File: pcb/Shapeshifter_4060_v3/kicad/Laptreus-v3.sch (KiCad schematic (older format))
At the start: 96 parts, among them SW1 TAB, SW10 O, SW11 P, SW12 BKSP, SW13 ESC, SW14 A, SW15 S, SW16 D, SW17 F, SW18 G, SW19 H, SW2 Q, SW20 J, SW21 K, SW22 L, SW23 ;, SW24 ENTER, SW25 SHIFT, SW26 Z, SW27 X, SW28 C, SW29 V, SW3 W, SW30 B, SW31 N, SW32 M, SW33 ,, SW34 ., SW35 /, SW36 SHIFT, SW37 CTRL/ESC, SW38 ALT/GRV, SW39 CMD, SW4 E, SW40 FN1, SW41 SHIFT, SW42 BKSP, SW43 ENTER, SW44 SPACE, SW45 LEFT, SW46 DOWN, SW47 UP, SW48 RIGHT, SW5 R, SW6 T, SW7 Y, SW8 U, SW9 I

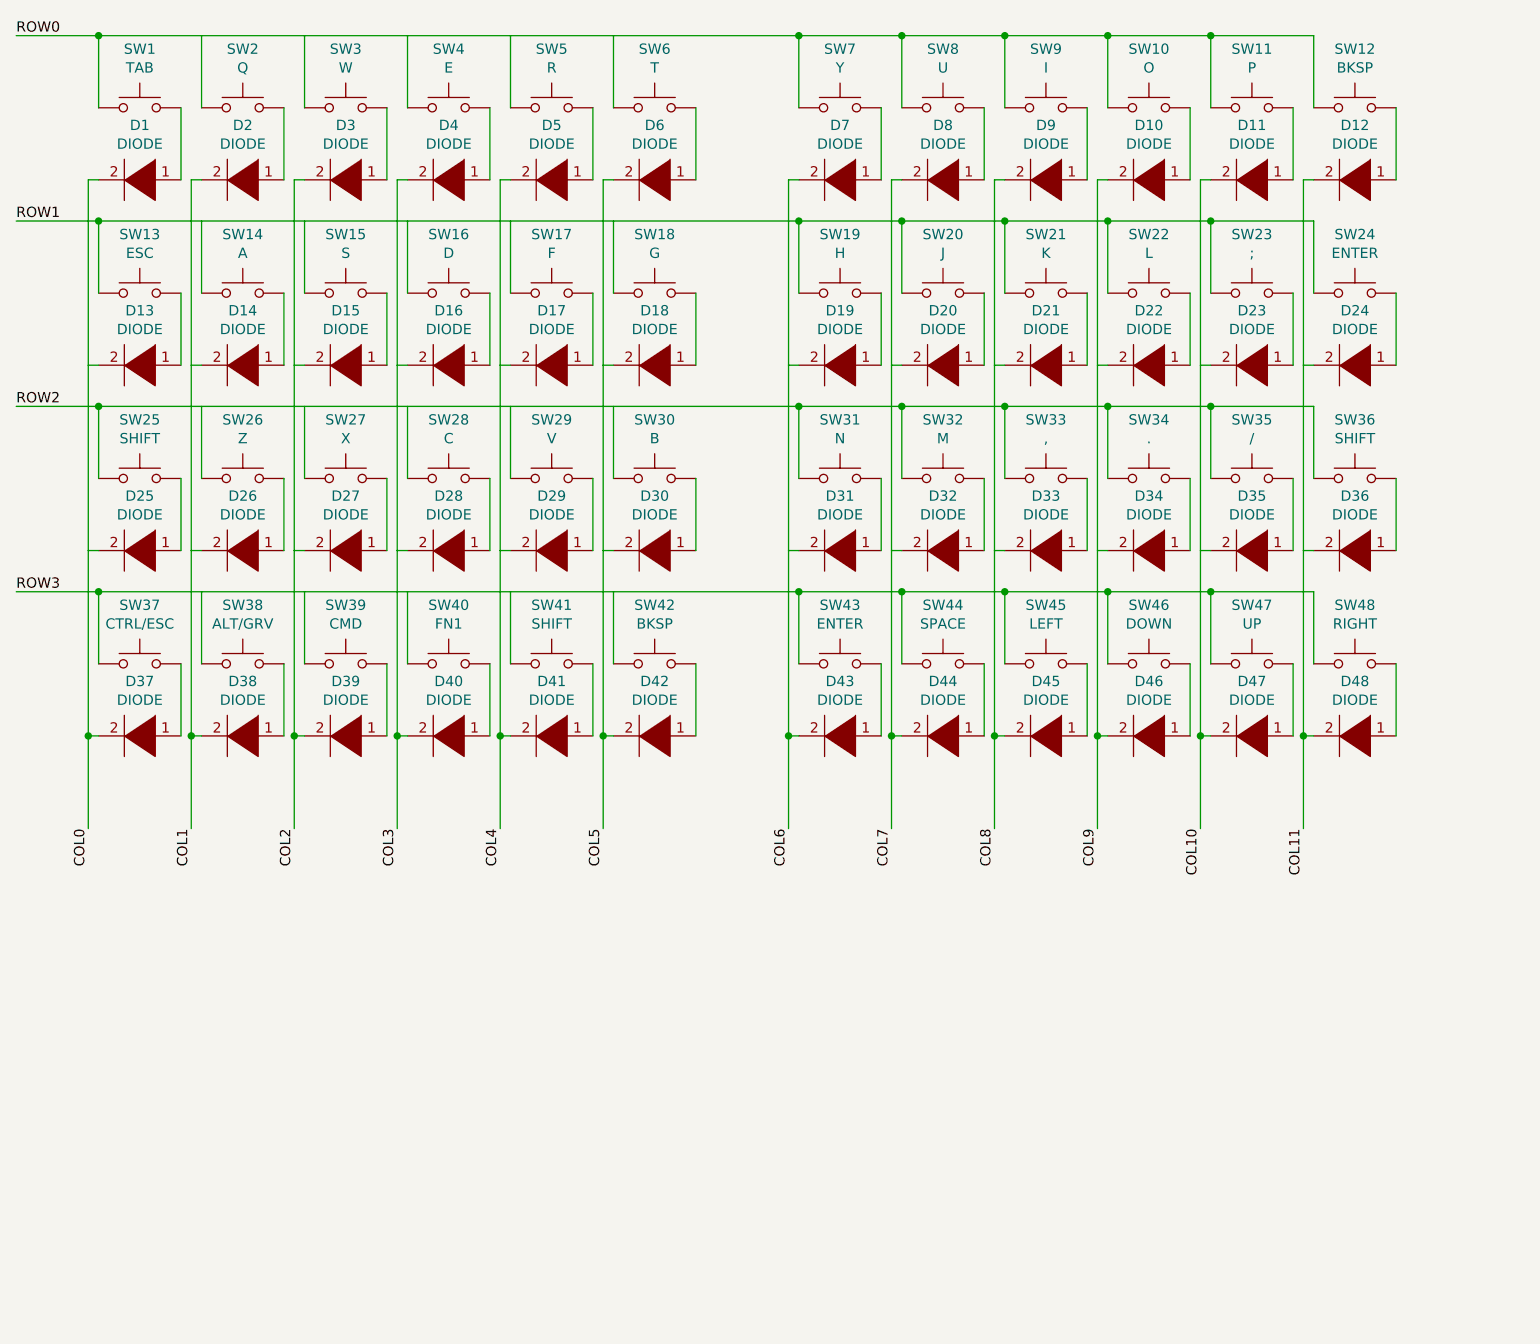
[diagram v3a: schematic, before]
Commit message: added fids/jumpers to schematic, fixed wiring typo, added pro micro fo otprint
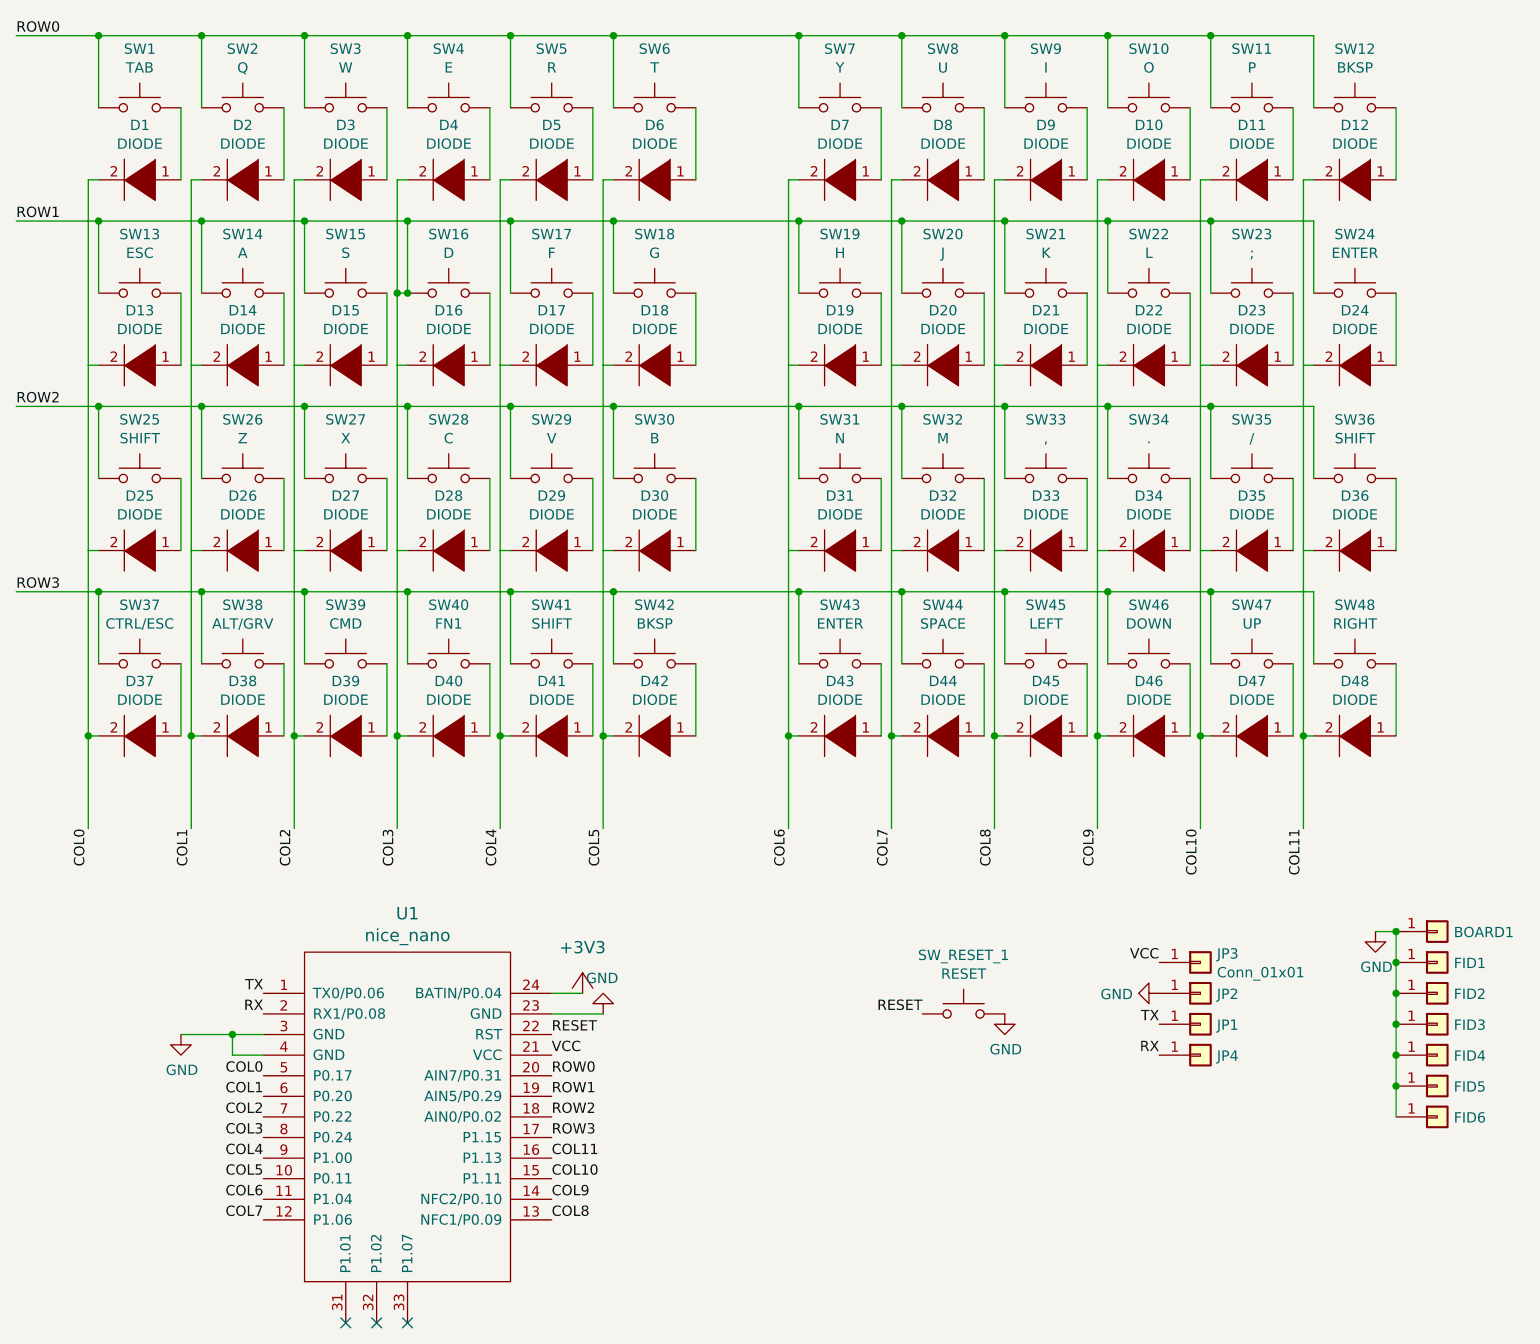
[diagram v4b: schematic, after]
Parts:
- added BOARD1: Conn_01x01, Kitsune-Footprints:60_percent_plus_tofu_no_center_holes, symbol Connector_Generic:Conn_01x01
- added FID1, FID2, FID3, FID4, FID5, FID6: Conn_01x01, Kitsune-Footprints:FIDUCIAL, symbol Connector_Generic:Conn_01x01
- added JP1, JP2, JP3, JP4: Conn_01x01, Kitsune-Footprints:1X01-CLEANBIG, symbol Connector_Generic:Conn_01x01
- added SW_RESET_1: RESET, Kitsune-Footprints:SW_SPST_B3U-1000P, symbol Kitsune-Symbols:SW_Push
- added U1: nice_nano, Kitsune-Footprints:nice_nano, symbol nice_nano:nice_nano
- SW13, SW14, SW23, SW24: footprint Kitsune-Footprints:Hybrid_Kailh_MX_Choc_Socket_Through_Hole_With_Diode -> Kitsune-Footprints:Hybrid_Kailh_MX_Choc_Socket_Through_Hole_With_Diode_No_Diode_Trace
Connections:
- net labels added: +3V3, GND, RESET, RX, TX, VCC
- wire segments 220 -> 255
- no-connect marks 0 -> 3

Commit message: Add nomask variant of nice nano, remove adhesives, add reset switch
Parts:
- SW13: footprint Kitsune-Footprints:Hybrid_Kailh_MX_Choc_Socket_Through_Hole_With_Diode_No_Diode_Trace -> Kitsune-Footprints:Hybrid_Kailh_MX_Choc_Socket_Through_Hole_With_Diode
- U1: footprint Kitsune-Footprints:nice_nano -> Kitsune-Footprints:nice_nano_no_Bcu_mask
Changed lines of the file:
@@
 F 0 "SW13" H 1500 2435 50  0000 C CNN
 F 1 "ESC" H 1500 2344 50  0000 C CNN
-F 2 "Kitsune-Footprints:Hybrid_Kailh_MX_Choc_Socket_Through_Hole_With_Diode_No_Diode_Trace" H 1500 2350 50  0001 C CNN
+F 2 "Kitsune-Footprints:Hybrid_Kailh_MX_Choc_Socket_Through_Hole_With_Diode" H 1500 2350 50  0001 C CNN
 F 3 "~" H 1500 2350 50  0001 C CNN
 	1    1500 2150
@@
 F 0 "U1" H 2800 7037 60  0000 C CNN
 F 1 "nice_nano" H 2800 6931 60  0000 C CNN
-F 2 "Kitsune-Footprints:nice_nano" V 3850 3600 60  0001 C CNN
+F 2 "Kitsune-Footprints:nice_nano_no_Bcu_mask" V 3850 3600 60  0001 C CNN
 F 3 "" V 3850 3600 60  0001 C CNN
 	1    2800 6100

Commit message: all components wired up!
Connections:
- net COL0: now also U1.6 (P0.20); no longer U1.5 (P0.17)
- net COL1: now also U1.5 (P0.17); no longer U1.6 (P0.20)
- net COL10: now also U1.8 (P0.24); no longer U1.15 (P1.11)
- net COL11: now also U1.7 (P0.22); no longer U1.16 (P1.13)
- net COL2: now also U1.16 (P1.13); no longer U1.7 (P0.22)
- net COL3: now also U1.15 (P1.11); no longer SW13.1, SW14.1, SW15.1, SW16.1, SW17.1, SW18.1, SW19.1, SW20.1, SW21.1, SW22.1, SW23.1, SW24.1, U1.19 (AIN5/P0.29), U1.8 (P0.24)
- net COL4: now also U1.14 (NFC2/P0.10); no longer U1.9 (P1.00)
- net COL5: now also U1.13 (NFC1/P0.09); no longer U1.10 (P0.11)
- net COL6: now also U1.12 (P1.06); no longer U1.11 (P1.04)
- net COL7: now also U1.11 (P1.04); no longer U1.12 (P1.06)
- net COL8: now also U1.10 (P0.11); no longer U1.13 (NFC1/P0.09)
- net COL9: now also U1.9 (P1.00); no longer U1.14 (NFC2/P0.10)
- new net ROW1: SW13.1, SW14.1, SW15.1, SW16.1, SW17.1, SW18.1, SW19.1, SW20.1, SW21.1, SW22.1, SW23.1, SW24.1, U1.19 (AIN5/P0.29)
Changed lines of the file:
@@
 Wire Wire Line
 	2800 1600 2750 1600
-Wire Wire Line
-	2750 1600 2750 2150
 $Comp
 L pspice:DIODE D5
@@
 	1    0    0    -1
 $EndComp
+Text Label 2100 6050 2    50   ~ 0
+COL0
 Text Label 2100 5950 2    50   ~ 0
-COL0
-Text Label 2100 6050 2    50   ~ 0
 COL1
+Text Label 3500 6350 0    50   ~ 0
+COL2
+Text Label 3500 6450 0    50   ~ 0
+COL3
+Text Label 3500 6550 0    50   ~ 0
+COL4
+Text Label 3500 6650 0    50   ~ 0
+COL5
+Text Label 2100 6650 2    50   ~ 0
+COL6
+Text Label 2100 6550 2    50   ~ 0
+COL7
+Text Label 2100 6450 2    50   ~ 0
+COL8
+Text Label 2100 6350 2    50   ~ 0
+COL9
+Text Label 2100 6250 2    50   ~ 0
+COL10
 Text Label 2100 6150 2    50   ~ 0
-COL2
-Text Label 2100 6250 2    50   ~ 0
-COL3
-Text Label 2100 6350 2    50   ~ 0
-COL4
-Text Label 2100 6450 2    50   ~ 0
-COL5
-Text Label 2100 6550 2    50   ~ 0
-COL6
-Text Label 2100 6650 2    50   ~ 0
-COL7
-Text Label 3500 6650 0    50   ~ 0
-COL8
-Text Label 3500 6550 0    50   ~ 0
-COL9
-Text Label 3500 6450 0    50   ~ 0
-COL10
-Text Label 3500 6350 0    50   ~ 0
 COL11
 Text Label 3500 6250 0    50   ~ 0
@@
 Connection ~ 2300 1800
 Wire Wire Line
-	2300 1800 2800 1800
-Wire Wire Line
-	2800 1800 2800 2150
-Wire Wire Line
-	2800 2150 2750 2150
-Connection ~ 2800 1800
-Wire Wire Line
-	2800 1800 3300 1800
-Connection ~ 2800 2150
-Connection ~ 2750 2150
-Wire Wire Line
-	2750 2150 2750 2500
-Wire Wire Line
 	3300 1800 3300 2150
 Connection ~ 3300 1800
@@
 	7500 5250 7600 5250
 Connection ~ 7600 5250
+Wire Wire Line
+	2300 1800 2800 1800
+Wire Wire Line
+	2750 1600 2750 2500
+Wire Wire Line
+	2800 2150 2800 1800
+Connection ~ 2800 1800
+Wire Wire Line
+	2800 1800 3300 1800
 $EndSCHEMATC

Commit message: Finished board. Wow. So much faster this time...
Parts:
- SW25, SW36: footprint Kitsune-Footprints:Hybrid_Kailh_MX_Choc_Socket_Through_Hole_With_Diode -> Kitsune-Footprints:Hybrid_Kailh_MX_Choc_Socket_Through_Hole_With_Diode_No_Diode_Trace
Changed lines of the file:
@@
 F 0 "SW36" H 7400 3335 50  0000 C CNN
 F 1 "SHIFT" H 7400 3244 50  0000 C CNN
-F 2 "Kitsune-Footprints:Hybrid_Kailh_MX_Choc_Socket_Through_Hole_With_Diode" H 7400 3250 50  0001 C CNN
+F 2 "Kitsune-Footprints:Hybrid_Kailh_MX_Choc_Socket_Through_Hole_With_Diode_No_Diode_Trace" H 7400 3250 50  0001 C CNN
 F 3 "~" H 7400 3250 50  0001 C CNN
 	1    7400 3050
@@
 F 0 "SW25" H 1500 3335 50  0000 C CNN
 F 1 "SHIFT" H 1500 3244 50  0000 C CNN
-F 2 "Kitsune-Footprints:Hybrid_Kailh_MX_Choc_Socket_Through_Hole_With_Diode" H 1500 3250 50  0001 C CNN
+F 2 "Kitsune-Footprints:Hybrid_Kailh_MX_Choc_Socket_Through_Hole_With_Diode_No_Diode_Trace" H 1500 3250 50  0001 C CNN
 F 3 "~" H 1500 3250 50  0001 C CNN
 	1    1500 3050

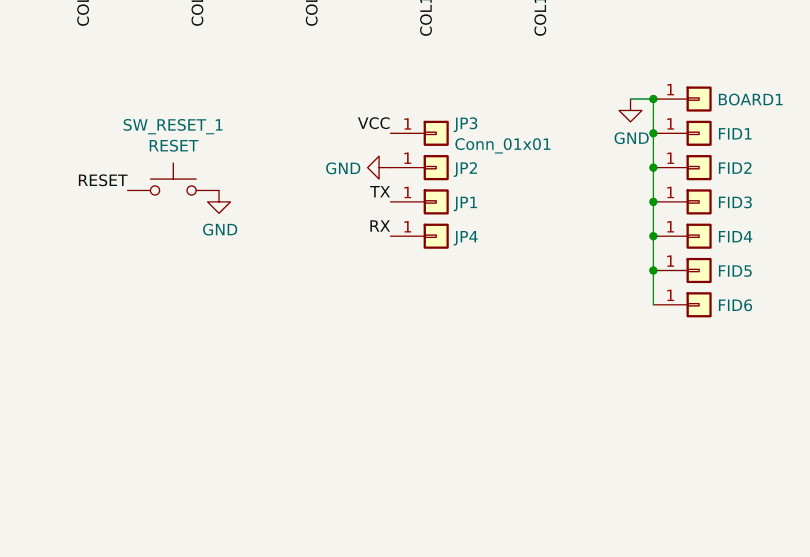
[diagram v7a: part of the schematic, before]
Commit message: Add pins for reset, add gerbers from last order, enlarged battery box
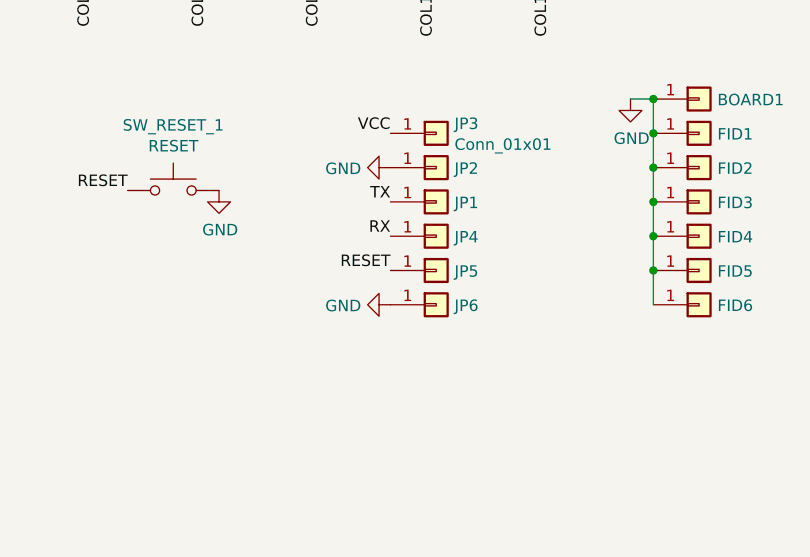
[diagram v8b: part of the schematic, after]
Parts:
- added JP5, JP6: Conn_01x01, Kitsune-Footprints:1X01-CLEANBIG, symbol Connector_Generic:Conn_01x01
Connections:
- net GND: now also JP6.1 (Pin_1)
- net RESET: now also JP5.1 (Pin_1)
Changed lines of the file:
@@
 Wire Wire Line
 	2800 1800 3300 1800
+$Comp
+L Connector_Generic:Conn_01x01 JP5
+U 1 1 6122D242
+P 6650 6000
+F 0 "JP5" H 6730 5996 50  0000 L CNN
+F 1 "Conn_01x01" H 6730 5951 50  0001 L CNN
+F 2 "Kitsune-Footprints:1X01-CLEANBIG" H 6650 6000 50  0001 C CNN
+F 3 "~" H 6650 6000 50  0001 C CNN
+	1    6650 6000
+	1    0    0    -1
+$EndComp
+$Comp
+L Connector_Generic:Conn_01x01 JP6
+U 1 1 6122D24C
+P 6650 6150
+F 0 "JP6" H 6730 6146 50  0000 L CNN
+F 1 "Conn_01x01" H 6730 6101 50  0001 L CNN
+F 2 "Kitsune-Footprints:1X01-CLEANBIG" H 6650 6150 50  0001 C CNN
+F 3 "~" H 6650 6150 50  0001 C CNN
+	1    6650 6150
+	1    0    0    -1
+$EndComp
+Text Label 6450 6000 2    50   ~ 0
+RESET
+$Comp
+L power:GND #PWR0107
+U 1 1 61275E31
+P 6450 6150
+F 0 "#PWR0107" H 6450 5900 50  0001 C CNN
+F 1 "GND" V 6455 6022 50  0000 R CNN
+F 2 "" H 6450 6150 50  0001 C CNN
+F 3 "" H 6450 6150 50  0001 C CNN
+	1    6450 6150
+	0    1    1    0
+$EndComp
 $EndSCHEMATC
